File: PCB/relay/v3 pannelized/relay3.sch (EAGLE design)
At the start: 16 parts, among them K1 JS-M1-9V-5, K2 JS-M1-9V-5, Q1 BSP75, X1 22-23-20315.08S, X2 22-23-20315.08S

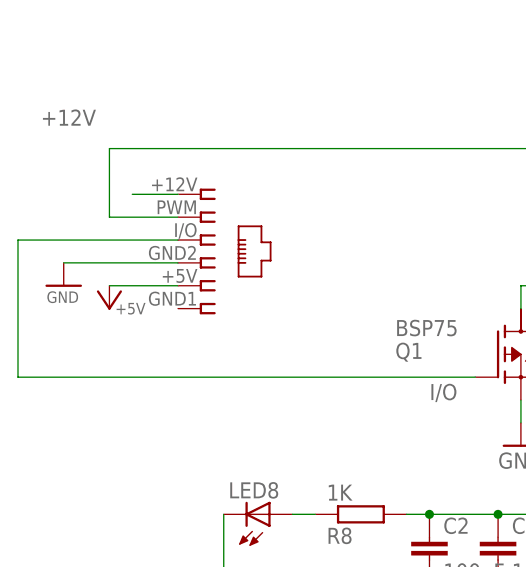
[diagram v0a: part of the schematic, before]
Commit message: created GERBER files for integratedBertha, anemometer, relay3, door locking pcb. Changed CAM processor file (corrected a bug in silk layer, added a job with univalle/EPFL logos on bottom side).
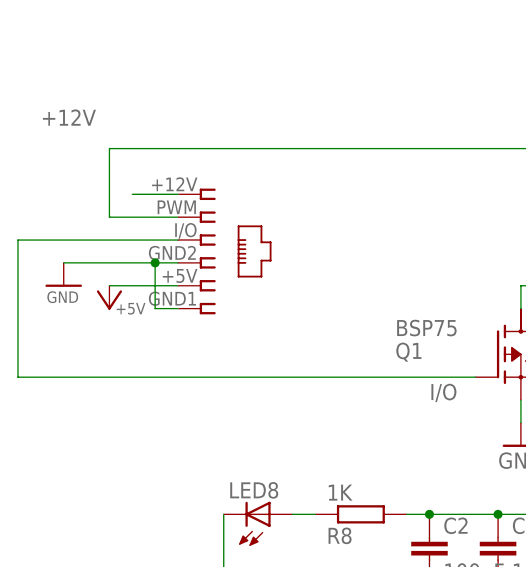
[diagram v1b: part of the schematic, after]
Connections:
- net GND: now also I/O_PWM.6
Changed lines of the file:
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@@
 <pinref part="I/O_PWM" gate="G$1" pin="4"/>
 <pinref part="GND1" gate="1" pin="GND"/>
-<wire x1="119.38" y1="175.26" x2="106.68" y2="175.26" width="0.1524" layer="91"/>
+<wire x1="119.38" y1="175.26" x2="116.84" y2="175.26" width="0.1524" layer="91"/>
+<pinref part="I/O_PWM" gate="G$1" pin="6"/>
+<wire x1="116.84" y1="175.26" x2="106.68" y2="175.26" width="0.1524" layer="91"/>
+<wire x1="119.38" y1="170.18" x2="116.84" y2="170.18" width="0.1524" layer="91"/>
+<wire x1="116.84" y1="170.18" x2="116.84" y2="175.26" width="0.1524" layer="91"/>
+<junction x="116.84" y="175.26"/>
 </segment>
 <segment>
